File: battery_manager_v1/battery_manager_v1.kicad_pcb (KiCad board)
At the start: 2 copper layers, 105.3 x 63 mm, 1 part

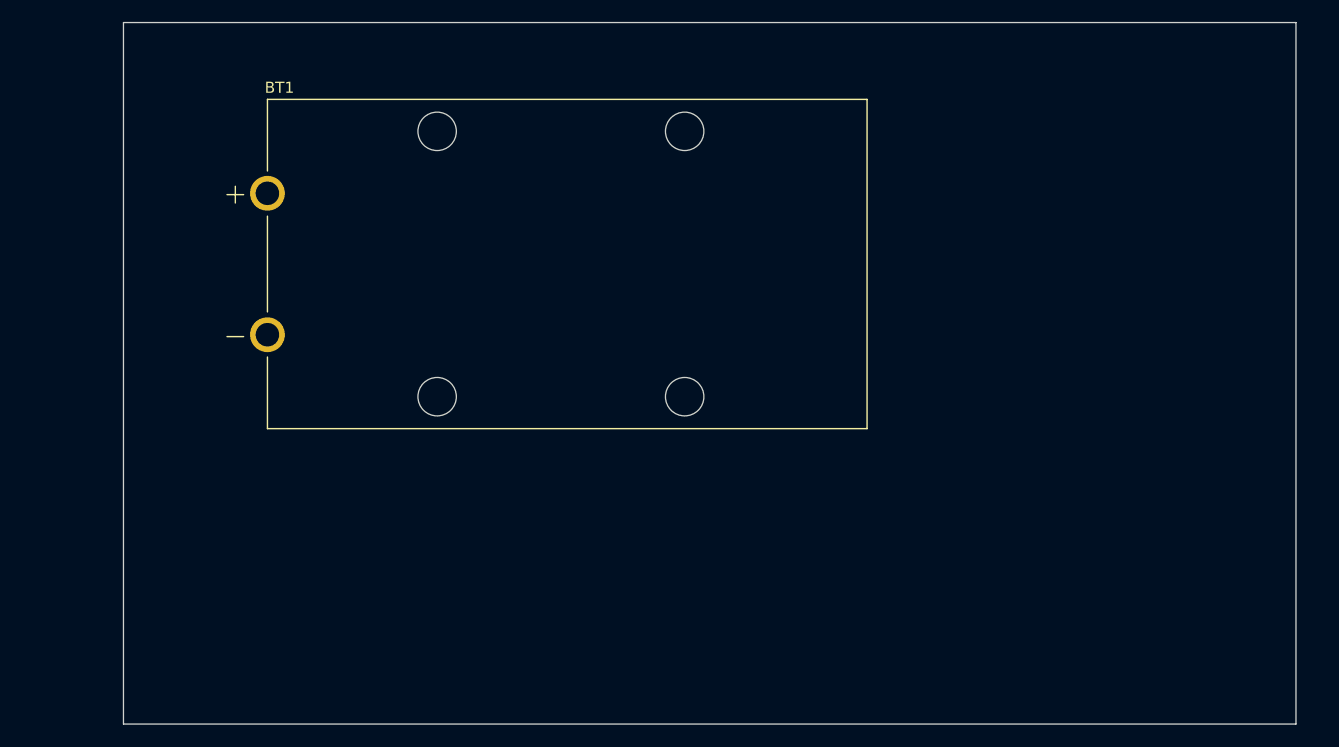
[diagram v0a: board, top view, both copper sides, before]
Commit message: Added Regulators etc.
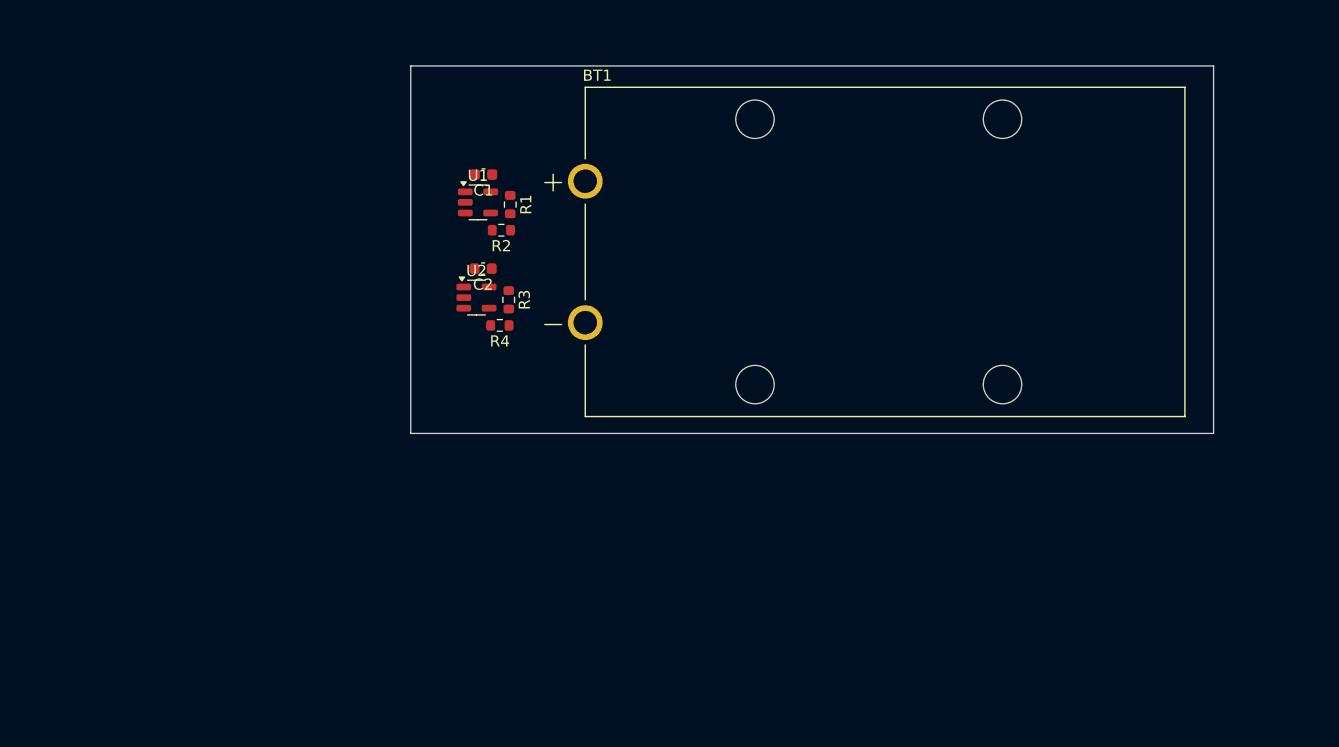
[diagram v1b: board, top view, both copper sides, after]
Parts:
- added C1: 1u, Capacitor_SMD:C_0603_1608Metric, F.Cu at (65.1, 43.0)
- added C2: 1u, Capacitor_SMD:C_0603_1608Metric, F.Cu at (65.1, 51.4)
- added R1: R_US, Resistor_SMD:R_0603_1608Metric, F.Cu at (67.5, 45.6)
- added R2: R_US, Resistor_SMD:R_0603_1608Metric, F.Cu at (66.7, 48.0)
- added R3: R_US, Resistor_SMD:R_0603_1608Metric, F.Cu at (67.4, 54.2)
- added R4: R_US, Resistor_SMD:R_0603_1608Metric, F.Cu at (66.6, 56.5)
- added U1: LT1761-SD, Package_TO_SOT_SMD:TSOT-23-5, F.Cu at (64.6, 45.5)
- added U2: LT1761-SD, Package_TO_SOT_SMD:TSOT-23-5, F.Cu at (64.5, 54.0)
- moved BT1 28.6 mm to (101.2, 49.9)
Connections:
- BT1 pad N: unconnected-(BT1-PadN) -> GND
- BT1 pad P: unconnected-(BT1-PadP) -> Net-(U1-VIN)
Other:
- board size 105.3 x 63 mm -> 72.1 x 33 mm

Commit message: V1 Final Before Update to V2
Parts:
- added H1: MountingHole_Pad, MountingHole:MountingHole_3.2mm_M3_DIN965_Pad_TopOnly, B.Cu at (68.0, 38.0)
- added H2: MountingHole_Pad, MountingHole:MountingHole_3.2mm_M3_DIN965_Pad_TopOnly, B.Cu at (134.0, 62.0)
- added H3: MountingHole_Pad, MountingHole:MountingHole_3.2mm_M3_DIN965_Pad_TopOnly, B.Cu at (134.0, 38.0)
- added J1: Conn_01x02, Connector_JST:JST_PH_S2B-PH-K_1x02_P2.00mm_Horizontal, B.Cu at (132.7, 53.0)
- added J2: Conn_01x02, Connector_JST:JST_PH_S2B-PH-K_1x02_P2.00mm_Horizontal, B.Cu at (132.7, 45.1)
- added SW1: SS-12F44-G5, LCSC Parts:SW-TH_SS-12F44-G5, B.Cu at (67.3, 49.5)
- BT1: footprint Battery Holder (Horizontal):BAT_1294 -> LCSC Parts:BAT_1294; moved to B.Cu
- moved C2 54.6 mm to (119.7, 50.2)
- moved R4 54.6 mm to (121.2, 55.3)
- moved R3 54.6 mm to (122.0, 53.0)
- moved U2 54.6 mm to (119.1, 52.8)
- moved R1 54.6 mm to (122.1, 45.9)
- moved R2 54.6 mm to (121.3, 48.1)
- moved C1 54.6 mm to (119.7, 43.1)
- moved U1 54.6 mm to (119.2, 45.6)
- moved BT1 0.91 mm to (100.3, 49.9), turned to 180 degrees
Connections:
- BT1 pad P: Net-(U1-VIN) -> Net-(BT1-PadP)
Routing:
- net Net-(U1-VIN): track 0.00 -> 69.5 mm
- net Net-(BT1-PadP): track 0.00 -> 61.1 mm
- net +5V: track 0.00 -> 18.8 mm
- net +8V: track 0.00 -> 14.6 mm
- net GND: track 0.00 -> 6.97 mm, vias 0 -> 6
- net Net-(U2-ADJ): track 0.00 -> 3.28 mm
- net Net-(U1-ADJ): track 0.00 -> 3.28 mm
- added copper zone on B.Cu, net GND
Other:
- board size 72.1 x 33 mm -> 76.1 x 34 mm

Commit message: Updates and first creation of gerbers
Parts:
- removed H3: MountingHole_Pad, MountingHole:MountingHole_3.2mm_M3_DIN965_Pad_TopOnly
- R1: value R_US -> 40.9k
- R2, R4: value R_US -> 10k
- R3: value R_US -> 65.5k
- moved H2 79.5 mm to (55.7, 76.1)
- moved J2 48.1 mm to (84.6, 47.5), turned to 0 degrees
- moved J1 48.0 mm to (86.6, 66.7), turned to 180 degrees
- moved BT1 47.8 mm to (53.0, 57.0)
- moved R1 47.8 mm to (74.8, 53.0)
- moved R2 47.8 mm to (74.0, 55.2)
- moved R3 47.8 mm to (74.7, 60.1)
- moved R4 47.8 mm to (73.9, 62.4)
- moved C2 47.8 mm to (72.4, 57.3)
- moved C1 47.8 mm to (72.4, 50.2)
- moved U1 47.8 mm to (71.9, 52.8)
- moved U2 47.8 mm to (71.8, 59.9)
- moved SW1 19.9 mm to (85.7, 57.1)
- moved H1 12.3 mm to (55.7, 38.1)
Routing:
- net Net-(BT1-PadP): track 61.1 -> 7.22 mm
- net Net-(U1-VIN): track 69.5 -> 28.7 mm, vias 0 -> 1
- net +8V: track 14.6 -> 18.6 mm
- net +5V: track 18.8 -> 15.2 mm
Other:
- board size 76.1 x 34 mm -> 65 x 46 mm
- board text added: "FR-4"
- board text added: "GND Plane"
- board text added: "Signal, SMD Fab"
- board text added: "Stackup:"
